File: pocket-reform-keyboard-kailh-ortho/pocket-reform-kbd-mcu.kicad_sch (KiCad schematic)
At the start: 177 parts, among them J1 Conn_01x06_Female, J2 USB, J3 UART, J4 AUX, SW65 SW_HWB, SW66 SW_RST, U1 SN74LV1T34DCK, U2 RP2040, U3 W25Q32JVSS, U4 MCP1700-3302E_SOT23, Y1 12MHz 18pF

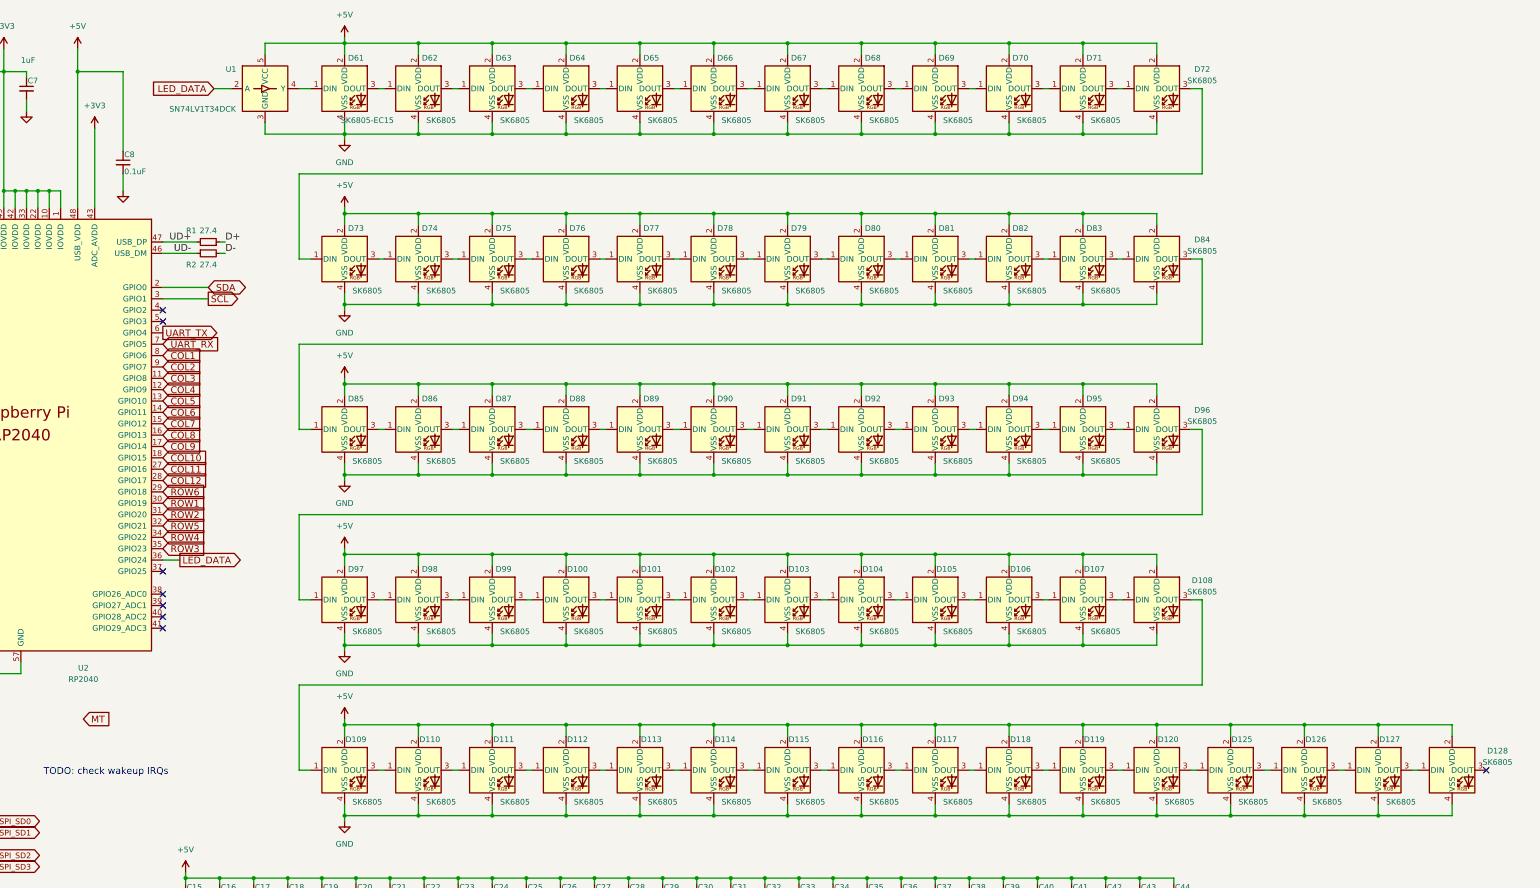
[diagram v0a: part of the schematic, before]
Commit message: keyboard: add D-1 version (beware, has hw bugs)
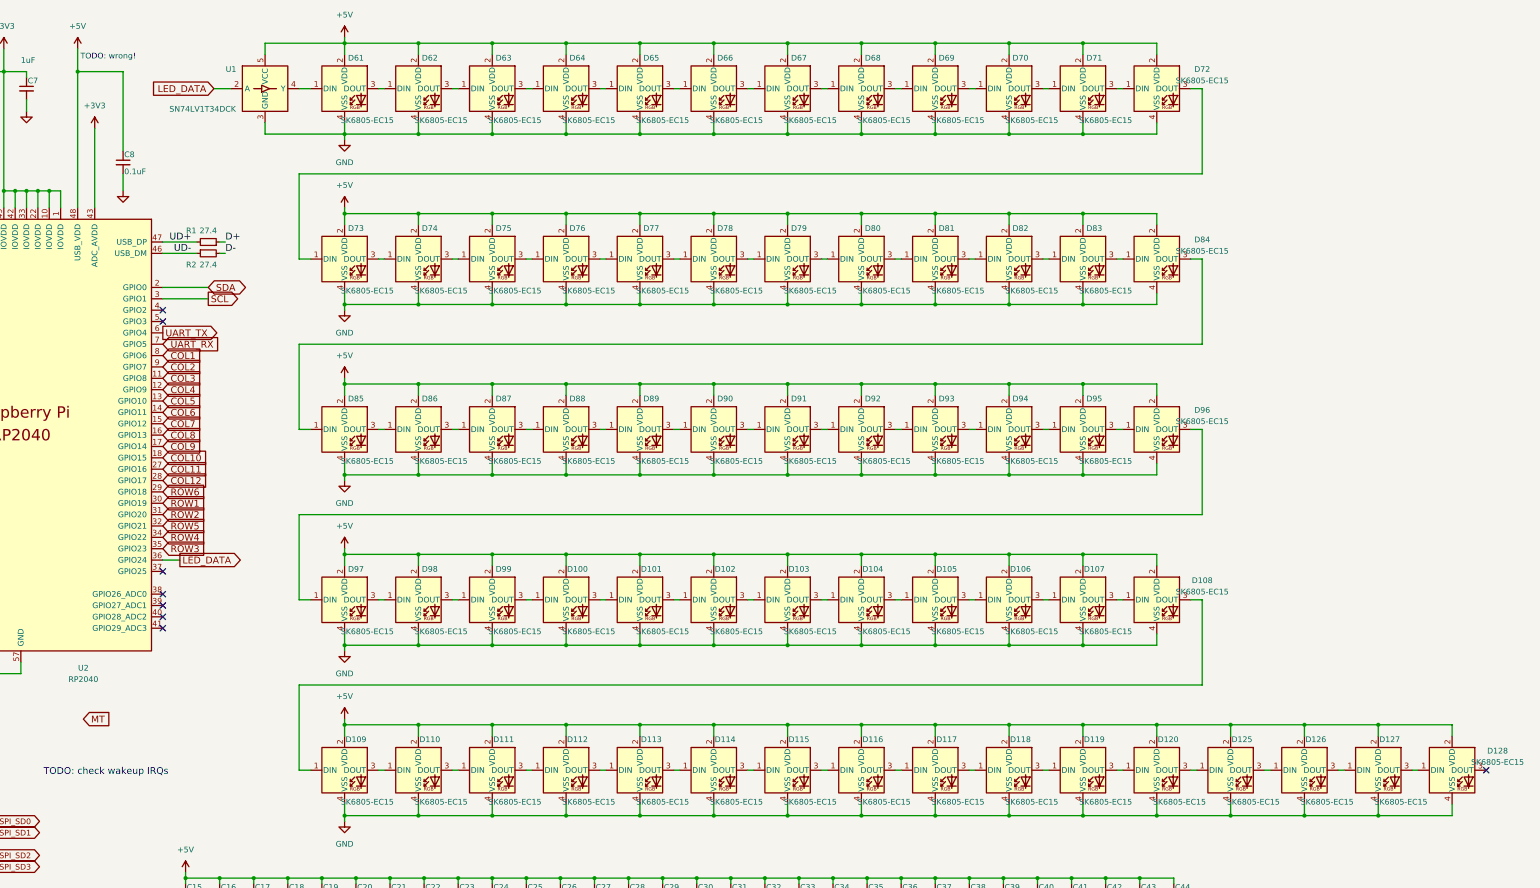
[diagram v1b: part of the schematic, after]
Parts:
- C75: LCSC (none) -> C14664; Manufacturer TDK -> Yageo; Manufacturer_No C1608X8L1C105K080AC -> CC0603KRX5R8BB105
- D100, D101, D102, D103, D104, D105, D106, D107, D108, D109, D110, D111, D112, D113, D114, D115, D116, D117, D118, D119, D120, D125, D126, D127, D128, D62, D63, D64, D65, D66, D67, D68, D69, D70, D71, D72, D73, D74, D75, D76, D77, D78, D79, D80, D81, D82, D83, D84, D85, D86, D87, D88, D89, D90, D91, D92, D93, D94, D95, D96, D97, D98, D99: value SK6805 -> SK6805-EC15; LCSC (none) -> C2890035; Manufacturer (none) -> OPSCO
- D61: LCSC (none) -> C2890035; Manufacturer (none) -> OPSCO
- GFX1, GFX2, H1, H10, H2, H3, H4, H5, H6, H7, H8, H9: LCSC (none) -> DNP
- J2, J3: LCSC (none) -> C265332
- J4: LCSC (none) -> C501491; Manufacturer Molex -> XFCN; Manufacturer_No 200528-0040 -> F1002-B-04-20T-R
- R8: LCSC (none) -> C95177; Manufacturer (none) -> Yageo; Manufacturer_No (none) -> RC0603JR-070RL
- U4: LCSC (none) -> C39051
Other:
- note added: "TODO: wrong!"

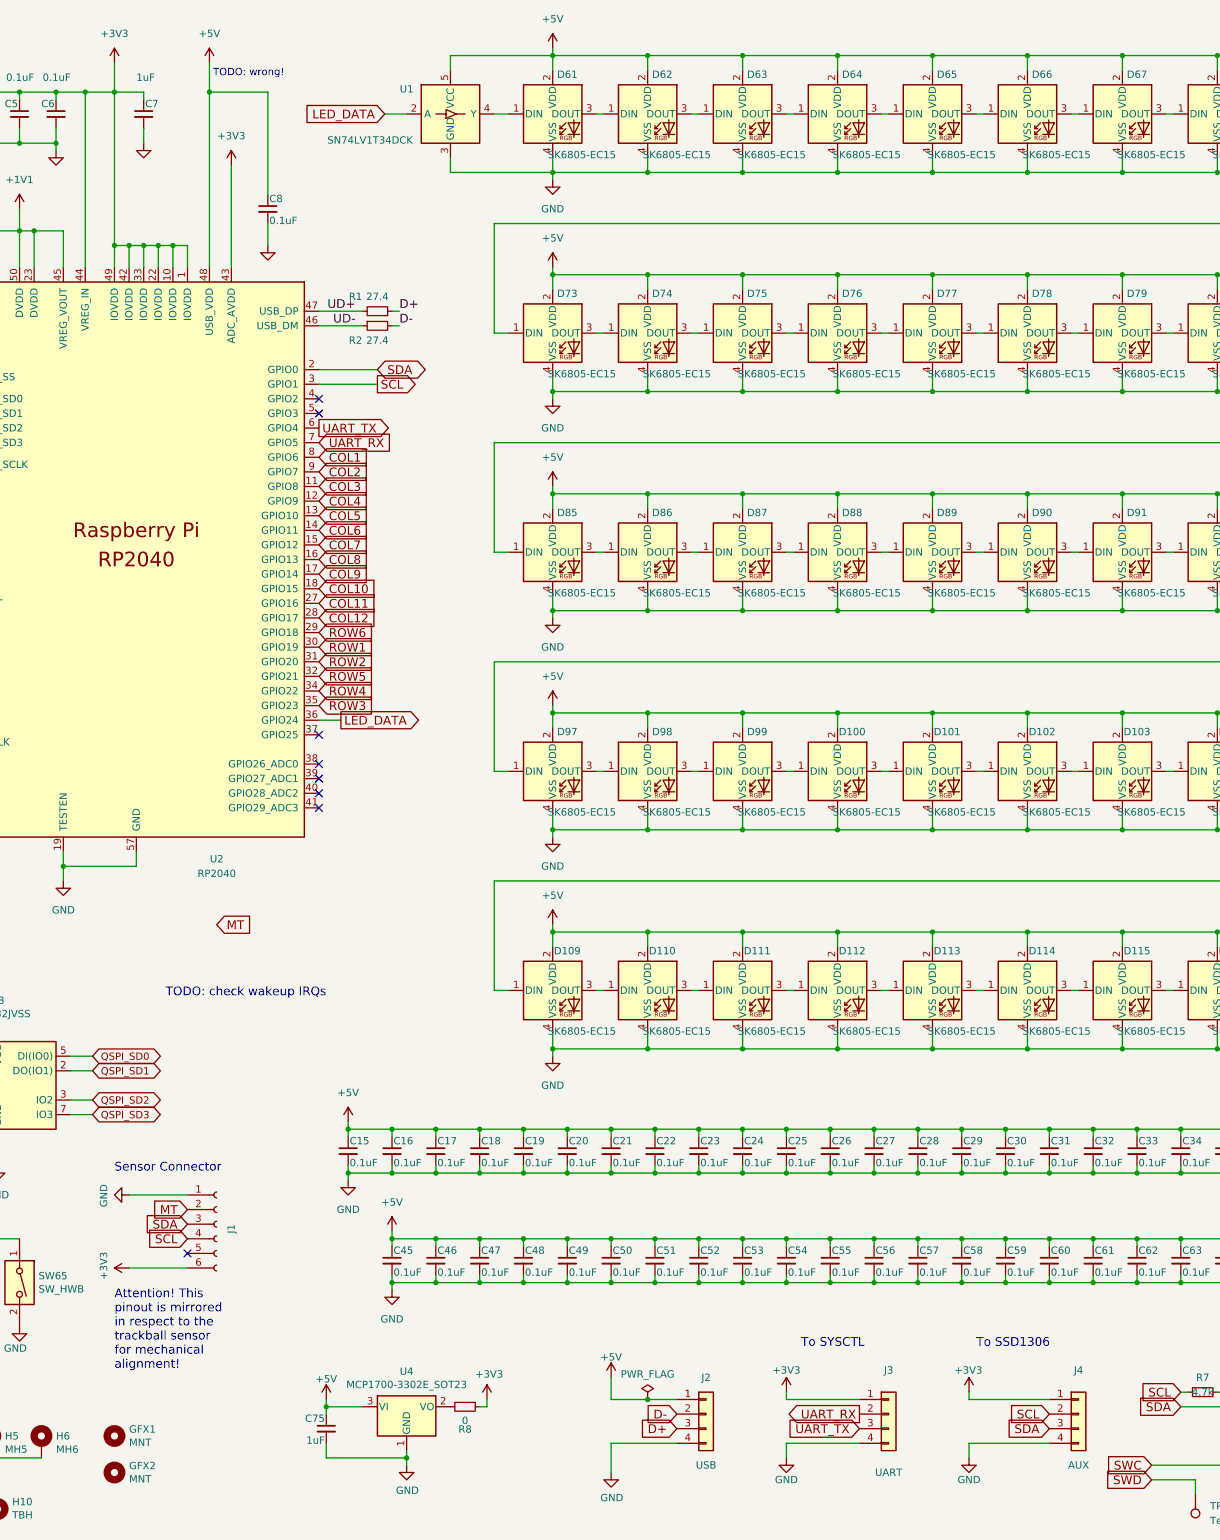
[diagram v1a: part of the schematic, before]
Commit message: keyboard d-2 done and exported for assembly
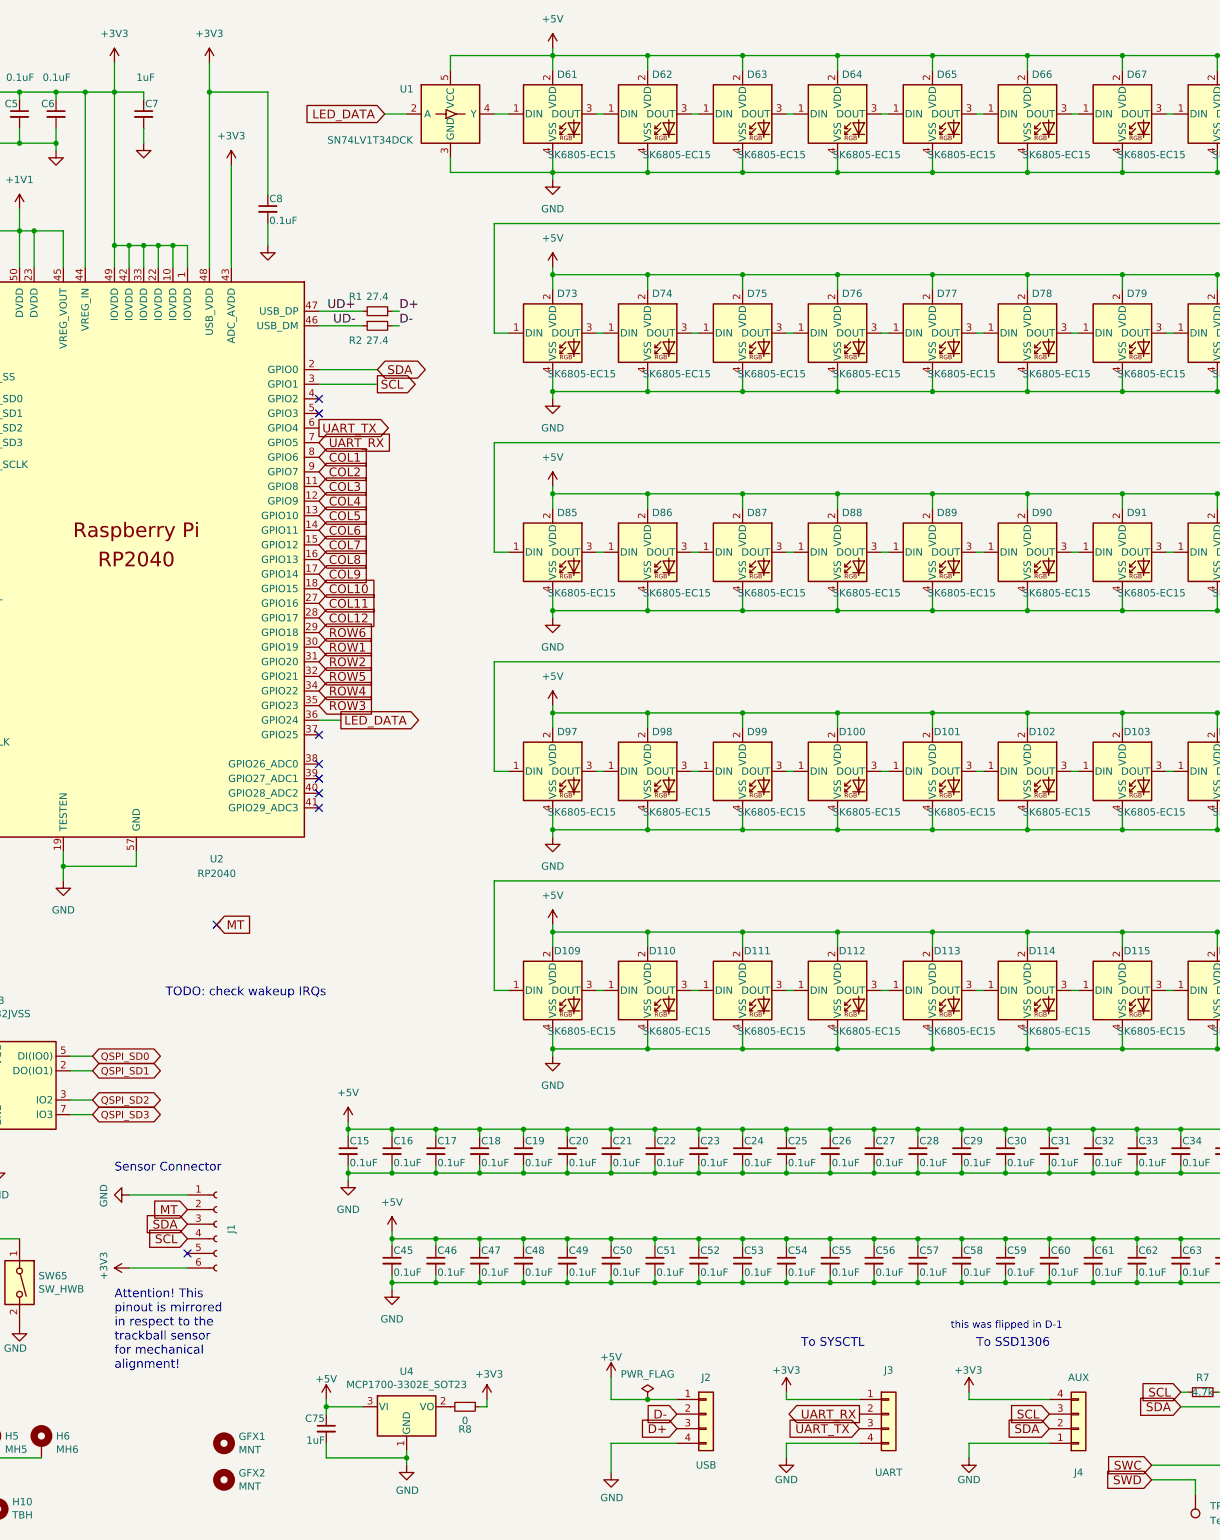
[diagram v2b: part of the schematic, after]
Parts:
- GFX2: footprint footprints:mpre-badge-d1 -> footprints:mpre-keyboard-badge-d2
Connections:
- net +3V3: now also C8.1, J4.4 (Pin_4), U2.48 (USB_VDD); no longer J4.1 (Pin_1)
- net +5V: no longer C8.1, U2.48 (USB_VDD)
- net GND: now also J4.1 (Pin_1); no longer J4.4 (Pin_4)
- net SCL: now also J4.3 (Pin_3); no longer J4.2 (Pin_2)
- net SDA: now also J4.2 (Pin_2); no longer J4.3 (Pin_3)
- no-connect marks 9 -> 10
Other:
- note added: "this was flipped in D-1"
- note removed: "TODO: wrong!"
- moved on the sheet: GFX1, GFX2
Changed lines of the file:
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@@
   (no_connect (at 118.11 86.36))
   (no_connect (at 118.11 142.24))
+  (no_connect (at 100.33 175.26))
   (wire (pts (xy 158.75 24.13) (xy 158.75 26.67))
     (stroke (width 0) (type default) (color 0 0 0 0))
@@
     (effects (font (size 1.524 1.524)) (justify left bottom))
   )
+  (text "this was flipped in D-1" (at 227.965 245.745 0)
+    (effects (font (size 1.27 1.27)) (justify left bottom))
+  )
   (text "To SSD1306" (at 232.41 248.92 0)
     (effects (font (size 1.524 1.524)) (justify left bottom))
@@
     (effects (font (size 1.524 1.524)) (justify left bottom))
   )
-  (text "TODO: wrong!" (at 99.695 27.94 0)
-    (effects (font (size 1.27 1.27)) (justify left bottom))
-  )
   (text "TODO: check wakeup IRQs" (at 91.44 187.96 0)
     (effects (font (size 1.524 1.524)) (justify left bottom))
@@
     (pin "1")
   )
-  (symbol (lib_id "Mechanical:MountingHole") (at 82.55 264.16 0) (unit 1)
+  (symbol (lib_id "Mechanical:MountingHole") (at 101.6 265.43 0) (unit 1)
     (in_bom yes) (on_board yes)
-    (property "Reference" "GFX1" (id 0) (at 85.09 262.9916 0)
+    (property "Reference" "GFX1" (id 0) (at 104.14 264.2616 0)
       (effects (font (size 1.27 1.27)) (justify left))
     )
-    (property "Value" "MNT" (id 1) (at 85.09 265.303 0)
+    (property "Value" "MNT" (id 1) (at 104.14 266.573 0)
       (effects (font (size 1.27 1.27)) (justify left))
     )
-    (property "Footprint" "footprints:pocket-reform" (id 2) (at 82.55 264.16 0)
+    (property "Footprint" "footprints:pocket-reform" (id 2) (at 101.6 265.43 0)
       (effects (font (size 1.27 1.27)) hide)
     )
-    (property "Datasheet" "~" (id 3) (at 82.55 264.16 0)
+    (property "Datasheet" "~" (id 3) (at 101.6 265.43 0)
       (effects (font (size 1.27 1.27)) hide)
     )
-    (property "LCSC" "DNP" (id 4) (at 82.55 264.16 0)
+    (property "LCSC" "DNP" (id 4) (at 101.6 265.43 0)
       (effects (font (size 1.27 1.27)) hide)
     )
   )
-  (symbol (lib_id "Connector_Generic:Conn_01x04") (at 250.19 260.35 0) (unit 1)
+  (symbol (lib_id "Connector_Generic:Conn_01x04") (at 250.19 262.89 0) (mirror x) (unit 1)
     (in_bom yes) (on_board yes)
-    (property "Reference" "J4" (id 0) (at 250.19 252.73 0))
-    (property "Value" "AUX" (id 1) (at 250.19 269.24 0))
-    (property "Footprint" "Connector_FFC-FPC:Molex_200528-0040_1x04-1MP_P1.00mm_Horizontal" (id 2) (at 250.19 260.35 0)
+    (property "Reference" "J4" (id 0) (at 250.19 270.51 0))
+    (property "Value" "AUX" (id 1) (at 250.19 254 0))
+    (property "Footprint" "Connector_FFC-FPC:Molex_200528-0040_1x04-1MP_P1.00mm_Horizontal" (id 2) (at 250.19 262.89 0)
       (effects (font (size 1.27 1.27)) hide)
     )
-    (property "Datasheet" "" (id 3) (at 250.19 260.35 0)
+    (property "Datasheet" "" (id 3) (at 250.19 262.89 0)
       (effects (font (size 1.27 1.27)) hide)
     )
-    (property "Manufacturer" "XFCN" (id 4) (at 250.19 260.35 0)
+    (property "Manufacturer" "XFCN" (id 4) (at 250.19 262.89 0)
       (effects (font (size 1.27 1.27)) hide)
     )
-    (property "Manufacturer_No" "F1002-B-04-20T-R" (id 5) (at 250.19 260.35 0)
+    (property "Manufacturer_No" "F1002-B-04-20T-R" (id 5) (at 250.19 262.89 0)
       (effects (font (size 1.27 1.27)) hide)
     )
-    (property "LCSC" "C501491" (id 6) (at 250.19 260.35 0)
+    (property "LCSC" "C501491" (id 6) (at 250.19 262.89 0)
       (effects (font (size 1.27 1.27)) hide)
     )
@@
     (pin "1")
   )
-  (symbol (lib_id "Mechanical:MountingHole") (at 82.55 270.51 0) (unit 1)
+  (symbol (lib_id "Mechanical:MountingHole") (at 101.6 271.78 0) (unit 1)
     (in_bom yes) (on_board yes)
-    (property "Reference" "GFX2" (id 0) (at 85.09 269.3416 0)
+    (property "Reference" "GFX2" (id 0) (at 104.14 270.6116 0)
       (effects (font (size 1.27 1.27)) (justify left))
     )
-    (property "Value" "MNT" (id 1) (at 85.09 271.653 0)
+    (property "Value" "MNT" (id 1) (at 104.14 272.923 0)
       (effects (font (size 1.27 1.27)) (justify left))
     )
-    (property "Footprint" "footprints:mpre-badge-d1" (id 2) (at 82.55 270.51 0)
+    (property "Footprint" "footprints:mpre-keyboard-badge-d2" (id 2) (at 101.6 271.78 0)
       (effects (font (size 1.27 1.27)) hide)
     )
-    (property "Datasheet" "~" (id 3) (at 82.55 270.51 0)
+    (property "Datasheet" "~" (id 3) (at 101.6 271.78 0)
       (effects (font (size 1.27 1.27)) hide)
     )
-    (property "LCSC" "DNP" (id 4) (at 82.55 270.51 0)
+    (property "LCSC" "DNP" (id 4) (at 101.6 271.78 0)
       (effects (font (size 1.27 1.27)) hide)
     )
@@
     (pin "4")
   )
+  (symbol (lib_id "power:+3V3") (at 99.06 25.4 0) (unit 1)
+    (in_bom yes) (on_board yes) (fields_autoplaced)
+    (property "Reference" "#PWR0101" (id 0) (at 99.06 29.21 0)
+      (effects (font (size 1.27 1.27)) hide)
+    )
+    (property "Value" "+3V3" (id 1) (at 99.06 20.32 0))
+    (property "Footprint" "" (id 2) (at 99.06 25.4 0)
+      (effects (font (size 1.27 1.27)) hide)
+    )
+    (property "Datasheet" "" (id 3) (at 99.06 25.4 0)
+      (effects (font (size 1.27 1.27)) hide)
+    )
+    (pin "1")
+  )
   (symbol (lib_id "pocket-reform-keyboard:SK6805-EC15") (at 290.83 148.59 0) (unit 1)
     (in_bom yes) (on_board yes)
@@
     (pin "4")
   )
-  (symbol (lib_id "power:+5V") (at 99.06 25.4 0) (unit 1)
-    (in_bom yes) (on_board yes) (fields_autoplaced)
-    (property "Reference" "#PWR03" (id 0) (at 99.06 29.21 0)
-      (effects (font (size 1.27 1.27)) hide)
-    )
-    (property "Value" "+5V" (id 1) (at 99.06 20.32 0))
-    (property "Footprint" "" (id 2) (at 99.06 25.4 0)
-      (effects (font (size 1.27 1.27)) hide)
-    )
-    (property "Datasheet" "" (id 3) (at 99.06 25.4 0)
-      (effects (font (size 1.27 1.27)) hide)
-    )
-    (pin "1")
-  )
   (symbol (lib_id "power:GND") (at 62.23 217.17 0) (unit 1)

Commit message: d-2 pcbs TODO
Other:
- note added: "TODO: LCSC: wrong pn! was 4k7"
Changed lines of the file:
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@@
     (effects (font (size 1.524 1.524)) (justify left bottom))
+  )
+  (text "TODO: LCSC: wrong pn! was 4k7" (at 25.4 107.95 0)
+    (effects (font (size 1.27 1.27)) (justify left bottom))
   )
   (text "Attention! This\npinout is mirrored\nin respect to the \ntrackball sensor\nfor mechanical\nalignment!"
@@
   (symbol (lib_id "Device:R_Small") (at 30.48 196.85 90) (unit 1)
     (in_bom yes) (on_board yes)
-    (property "Reference" "R5" (id 0) (at 29.972 194.818 90)
-      (effects (font (size 1.27 1.27)) (justify left))
-    )
+    (property "Reference" "R5" (id 0) (at 29.972 199.898 90)
+      (effects (font (size 1.27 1.27)) (justify left))
+    )

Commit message: keyboard D-3: production snapshot
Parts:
- D100, D101, D102, D103, D104, D105, D106, D107, D108, D109, D110, D111, D112, D113, D114, D115, D116, D117, D118, D119, D120, D125, D126, D127, D128, D61, D62, D63, D64, D65, D66, D67, D68, D69, D70, D71, D72, D73, D74, D75, D76, D77, D78, D79, D80, D81, D82, D83, D84, D85, D86, D87, D88, D89, D90, D91, D92, D93, D94, D95, D96, D97, D98, D99: Manufacturer_No (none) -> SK6805-EC15
- GFX2: footprint footprints:mpre-keyboard-badge-d2 -> footprints:mpre-keyboard-badge-d3
- J2, J3: footprint Connector_JST:JST_PH_S4B-PH-SM4-TB_1x04-1MP_P2.00mm_Horizontal -> Connector_JST:JST_SH_SM04B-SRSS-TB_1x04-1MP_P1.00mm_Horizontal; LCSC C265332 -> C160404; Manufacturer_No S4B-PH-SM4-TB(LF)(SN) -> SM04B-SRSS-TB(LF)(SN)
- R3: LCSC C105428 -> C14676; Manufacturer_No RC0603FR-074K7L -> RC0603JR-071KL
